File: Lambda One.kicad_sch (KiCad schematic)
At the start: 0 parts

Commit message: added 65xxx
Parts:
- added U1: W65C816SxP, Package_DIP:DIP-40_W15.24mm, symbol 65xx-library:W65C816SxP
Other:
- company: (none) -> Embrace
- title: (none) -> Lambda One
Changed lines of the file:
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@@
 	(generator_version "9.0")
 	(paper "A4")
+	(title_block
+		(title "Lambda One")
+		(date "2026-07-11")
+		(rev "v1")
+		(company "Embrace")
+	)
+	(symbol
+		(lib_id "65xx-library:W65C816SxP")
+		(at 113.03 96.52 0)
+		(unit 1)
+		(exclude_from_sim no)
+		(in_bom yes)
+		(on_board yes)
+		(dnp no)
+		(fields_autoplaced yes)
+		(property "Reference" "U1"
+			(at 115.1733 55.88 0)
+			(effects
+				(font
+					(size 1.27 1.27)
+				)
+				(justify left)
+			)
+		)
+		(property "Value" "W65C816SxP"
+			(at 115.1733 58.42 0)
+			(effects
+				(font
+					(size 1.27 1.27)
+				)
+				(justify left)
+			)
+		)
+		(property "Footprint" "Package_DIP:DIP-40_W15.24mm"
+			(at 113.03 45.72 0)
+			(effects
+				(font
+					(size 1.27 1.27)
+				)
+				(hide yes)
+			)
+		)
+		(property "Datasheet" "http://www.westerndesigncenter.com/wdc/documentation/w65c816s.pdf"
+			(at 113.03 48.26 0)
+			(effects
+				(font
+					(size 1.27 1.27)
+				)
+				(hide yes)
+			)
+		)
+		(property "Description" "8/16-bit CMOS General Purpose Microprocessor, DIP-40"
+			(at 113.03 96.52 0)
+			(effects
+				(font
+					(size 1.27 1.27)
+				)
+				(hide yes)
+			)
+		)
+		(pin "11"
+		)
+		(pin "13"
+		)
+		(pin "31"
+		)
+		(pin "19"
+		)
+		(pin "16"
+		)
+		(pin "29"
+		)
+		(pin "4"
+		)
+		(pin "3"
+		)
+		(pin "37"
+		)
+		(pin "21"
+		)
+		(pin "12"
+		)
+		(pin "17"
+		)
+		(pin "7"
+		)
+		(pin "39"
+		)
+		(pin "27"
+		)
+		(pin "24"
+		)
+		(pin "2"
+		)
+		(pin "40"
+		)
+		(pin "25"
+		)
+		(pin "15"
+		)
+		(pin "8"
+		)
+		(pin "33"
+		)
+		(pin "1"
+		)
+		(pin "18"
+		)
+		(pin "26"
+		)
+		(pin "9"
+		)
+		(pin "14"
+		)
+		(pin "10"
+		)
+		(pin "35"
+		)
+		(pin "22"
+		)
+		(pin "5"
+		)
+		(pin "36"
+		)
+		(pin "32"
+		)
+		(pin "23"
+		)
+		(pin "20"
+		)
+		(pin "28"
+		)
+		(pin "34"
+		)
+		(pin "6"
+		)
+		(pin "38"
+		)
+		(pin "30"
+		)
+		(instances
+			(project "Lambda One"
+				(path "/73ea9964-373f-4fdc-b03e-f532cf836c0d"
+					(reference "U1")
+					(unit 1)
+				)
+			)
+		)
+	)
 	(sheet_instances
 		(path "/"

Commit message: added ram and rom
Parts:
- added U2: 28C256, symbol Memory_EEPROM:28C256
- added U3: ATF22V10C, MODULE, symbol ATF22V10C:ATF22V10C
- added U4: AS6C1008-xxP, Package_DIP:DIP-32_W15.24mm, symbol Memory_RAM:AS6C1008-xxP
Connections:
- net Addr1: now reaches U1.10 (A1)
- net Addr1: now also U2.9 (A1), U4.11 (A1)
- net Addr2: now reaches U1.11 (A2)
- net Addr2: now also U2.8 (A2), U4.10 (A2)
- net Addr3: now reaches U1.12 (A3)
- net Addr3: now also U2.7 (A3), U4.9 (A3)
- net Addr4: now reaches U1.13 (A4)
- net Addr4: now also U2.6 (A4), U4.8 (A4)
- net Addr5: now reaches U1.14 (A5)
- net Addr5: now also U2.5 (A5), U3.2 (IN0), U4.7 (A5)
- net Addr6: now reaches U1.15 (A6)
- net Addr6: now also U2.4 (A6), U3.3 (IN1), U4.6 (A6)
- net Addr7: now reaches U1.16 (A7)
- net Addr7: now also U2.3 (A7), U3.4 (IN2), U4.5 (A7)
- net Addr8: now reaches U1.17 (A8)
- net Addr8: now also U2.25 (A8), U3.5 (IN3), U4.27 (A8)
- net Addr9: now reaches U1.18 (A9)
- net Addr9: now also U2.24 (A9), U3.6 (IN4), U4.26 (A9)
- net Addr10: now reaches U1.19 (A10)
- net Addr10: now also U2.21 (A10), U3.7 (IN5), U4.23 (A10)
- net Addr11: now reaches U1.20 (A11)
- net Addr11: now also U2.23 (A11), U3.8 (IN6), U4.25 (A11)
- net GND: now reaches U1.21 (VSS)
- net GND: now also U2.14 (GND), U2.22 (~{OE}), U4.16 (GND), U4.24 (~{OE})
- net Addr12: now reaches U1.22 (A12)
- net Addr12: now also U2.2 (A12), U3.9 (IN7), U4.4 (A12)
- net Addr13: now reaches U1.23 (A13)
- net Addr13: now also U2.26 (A13), U3.10 (IN8), U4.28 (A13)
- net Addr14: now reaches U1.24 (A14)
- net Addr14: now also U2.1 (A14), U3.11 (IN9), U4.3 (A14)
- net Addr15: now reaches U1.25 (A15)
- net Addr15: now also U3.13 (IN10), U4.31 (A15)
- net D7: now reaches U1.26 (D7)
- net D7: now also U2.19 (D7), U4.21 (DQ7)
- net D6: now reaches U1.27 (D6)
- net D6: now also U2.18 (D6), U4.20 (DQ6)
- net D5: now reaches U1.28 (D5)
- net D5: now also U2.17 (D5), U4.19 (DQ5)
- net D4: now reaches U1.29 (D4)
- net D4: now also U2.16 (D4), U4.18 (DQ4)
- net D3: now reaches U1.30 (D3)
- net D3: now also U2.15 (D3), U4.17 (DQ3)
- net D2: now reaches U1.31 (D2)
- net D2: now also U2.13 (D2), U4.15 (DQ2)
- net D1: now reaches U1.32 (D1)
- net D1: now also U2.12 (D1), U4.14 (DQ1)
- net D0: now reaches U1.33 (D0)
- net D0: now also U2.11 (D0), U4.13 (DQ0)
- net R/W: now reaches U1.34 (R/~{W})
- net R/W: now also U4.29 (~{WE})
- net +5V: now reaches U1.8 (VDD)
- net +5V: now also U2.27 (~{WE}), U2.28 (VCC), U4.30 (CS2/CE2), U4.32 (VCC)
- net Addr0: now reaches U1.9 (A0)
- net Addr0: now also U2.10 (A0), U4.12 (A0)
- new net RAM_CS: U3.15 (IO8), U4.22 (~{CS1}/~{CE1})
- new net ROM_CS: U2.20 (~{CS}), U3.14 (IO9)

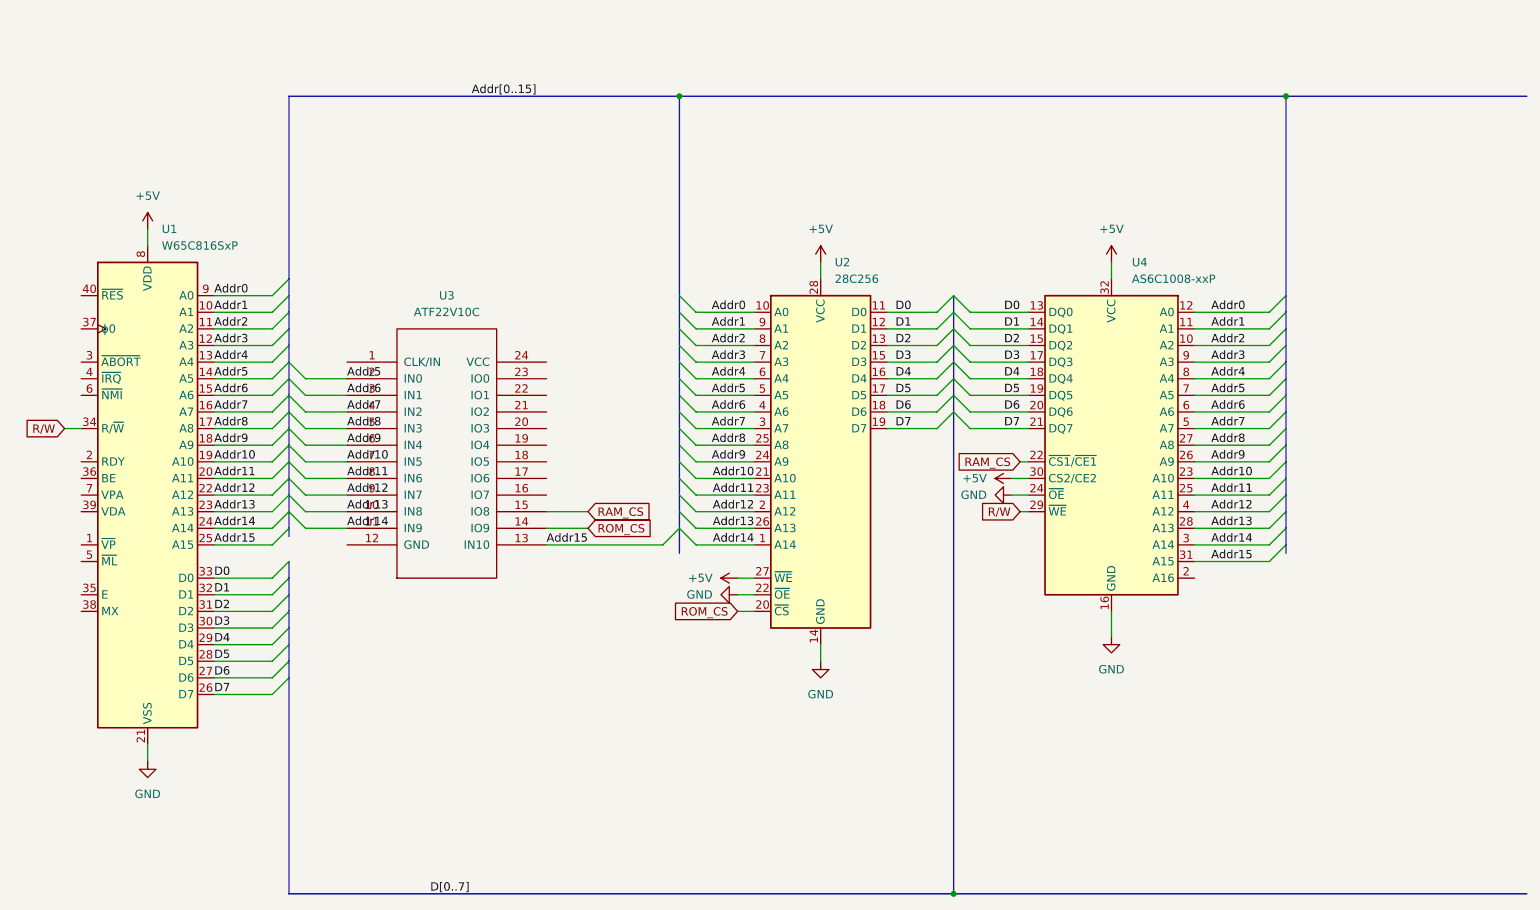
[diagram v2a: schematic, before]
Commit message: Added bank switching
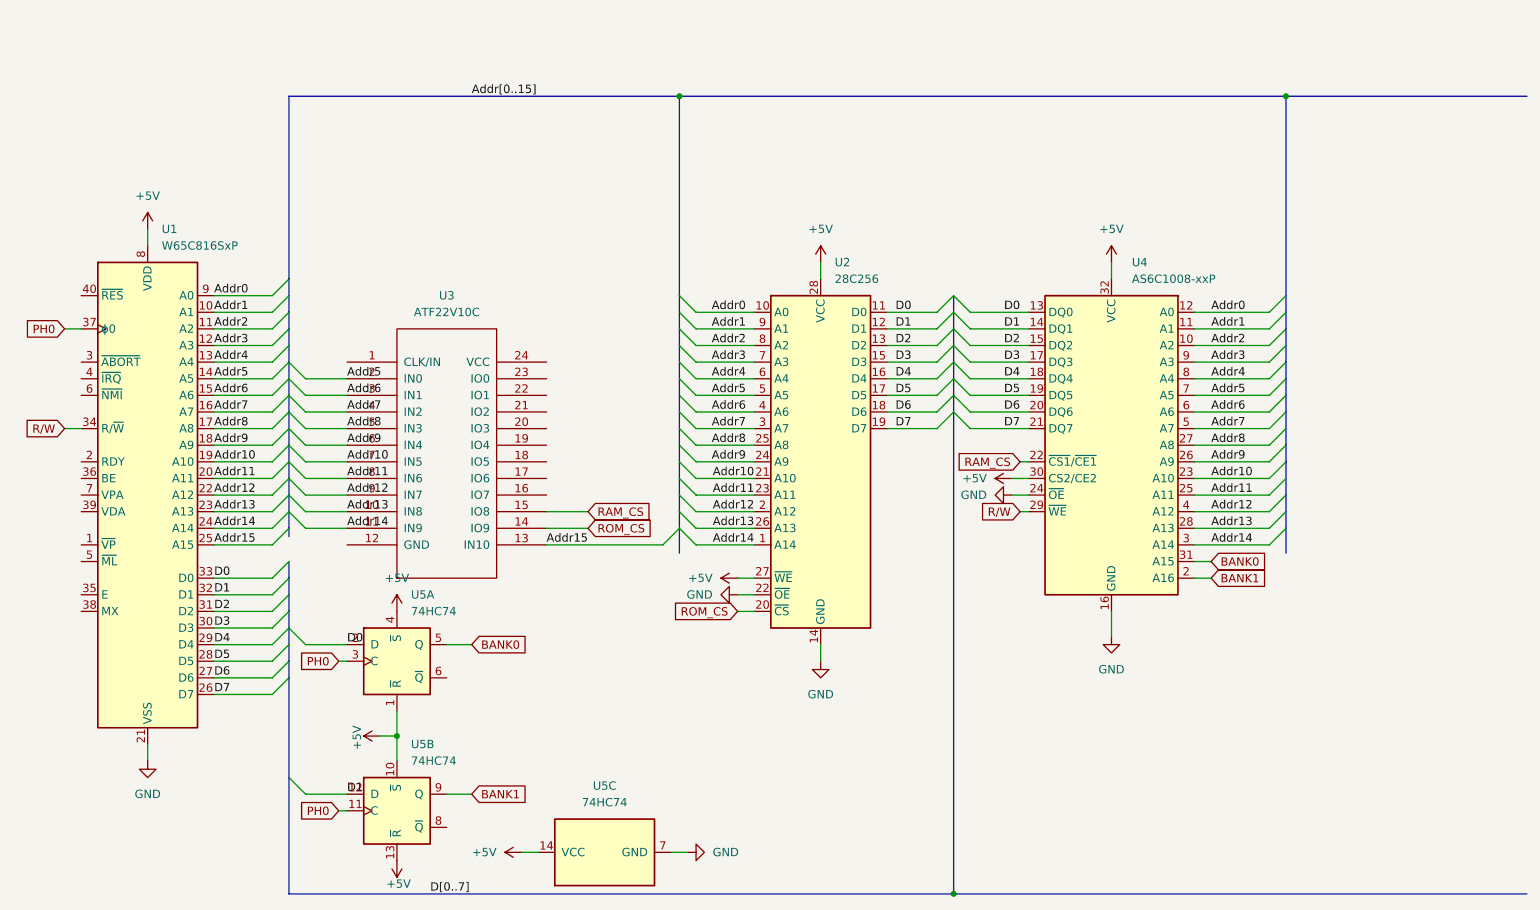
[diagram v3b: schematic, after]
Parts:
- added U5: 74HC74, symbol 74xx:74HC74
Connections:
- net +5V: now also U5.1 (~{R}), U5.10 (~{S}), U5.13 (~{R}), U5.14 (VCC), U5.4 (~{S})
- net Addr15: no longer U4.31 (A15)
- net D0: now also U5.2 (D)
- net D1: now also U5.12 (D)
- net GND: now also U5.7 (GND)
- net BANK1: now reaches U4.2 (A16)
- net BANK1: now also U5.9 (Q)
- net PH0: now reaches U1.37 (ϕ0)
- net PH0: now also U5.11 (C), U5.3 (C)
- new net BANK0: U4.31 (A15), U5.5 (Q)

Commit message: Added reset button
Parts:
- added IC1: 01, symbol cern_ds1813_10_t_r:DS1813
- added SW1: SW_Push, symbol Switch:SW_Push
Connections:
- net +5V: now also IC1.2 (VCC); no longer U5.1 (~{R}), U5.10 (~{S})
- net GND: now also IC1.3 (GND), SW1.1
- net MR: now reaches U1.40 (~{RES})
- net MR: now also U5.1 (~{R}), U5.10 (~{S}), IC1.1 (~{RST}), SW1.2
